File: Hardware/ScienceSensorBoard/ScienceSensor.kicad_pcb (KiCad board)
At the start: 2 copper layers, 2 x 2 mm, 93 parts, among them J1 Conn_02x03_Counter_Clockwise, J2 RJ45_LED_Shielded, Q1 SI4156DY, Q10 BSS138, Q11 SI4156DY, Q2 SI4156DY, Q3 SI4156DY, Q4 BSS138, Q5 BSS138, Q6 BSS138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

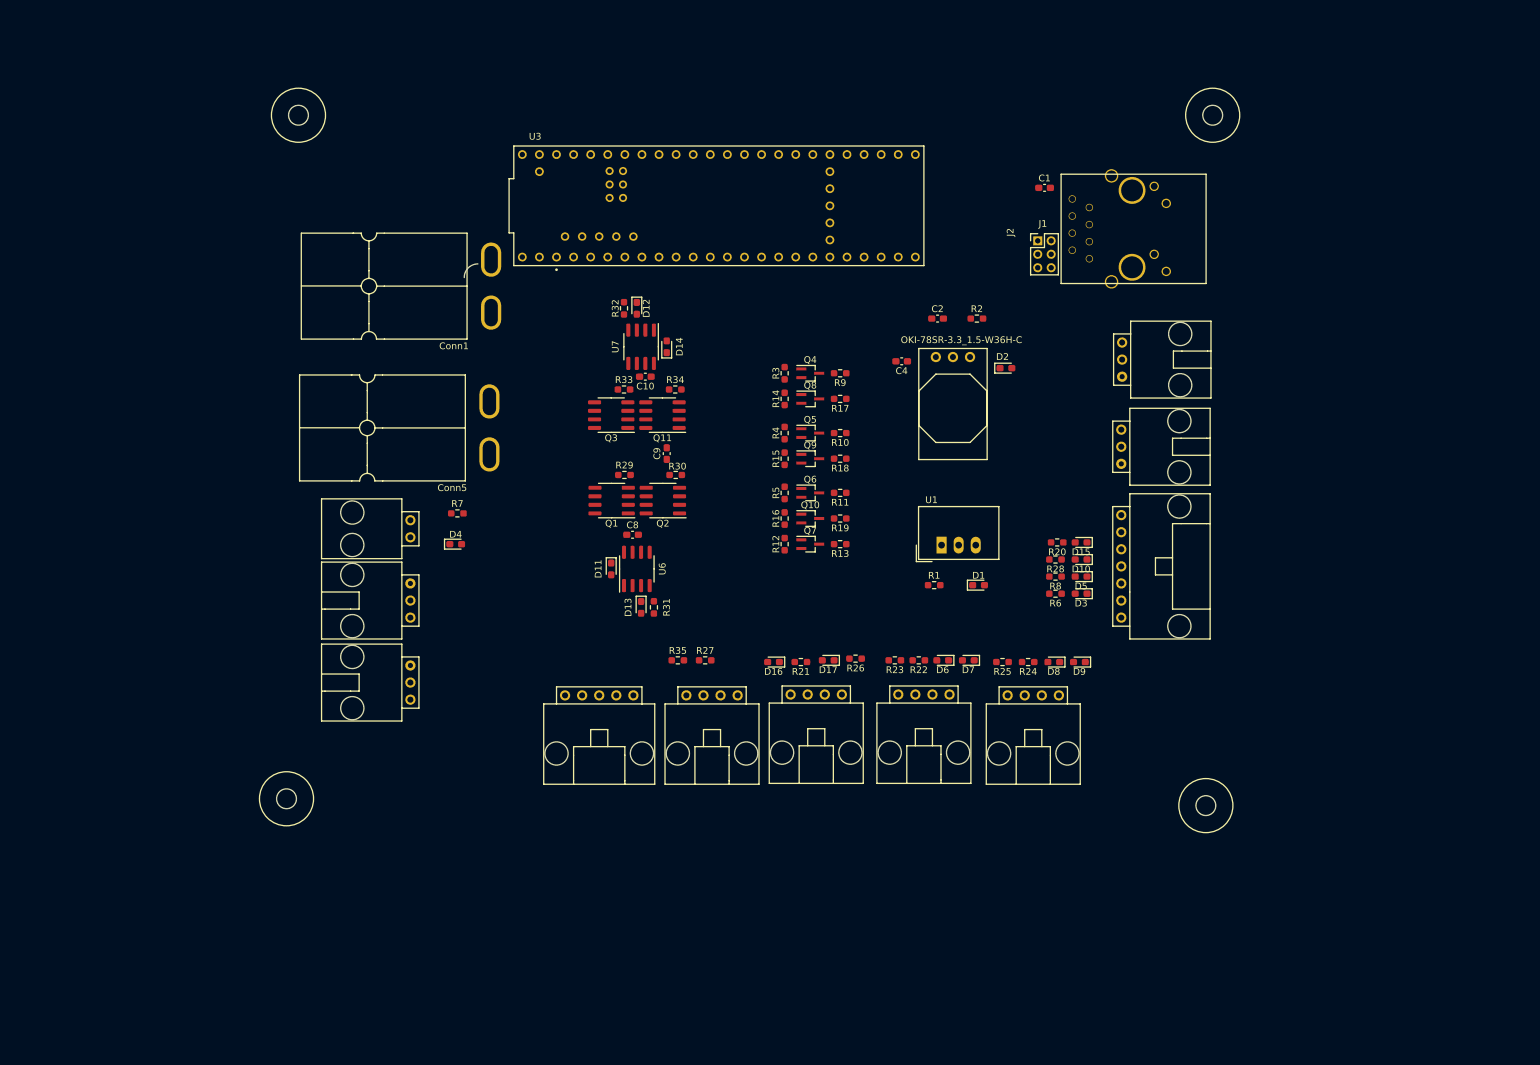
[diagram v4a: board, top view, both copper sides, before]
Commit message: Layout Edge Cuts and Organization
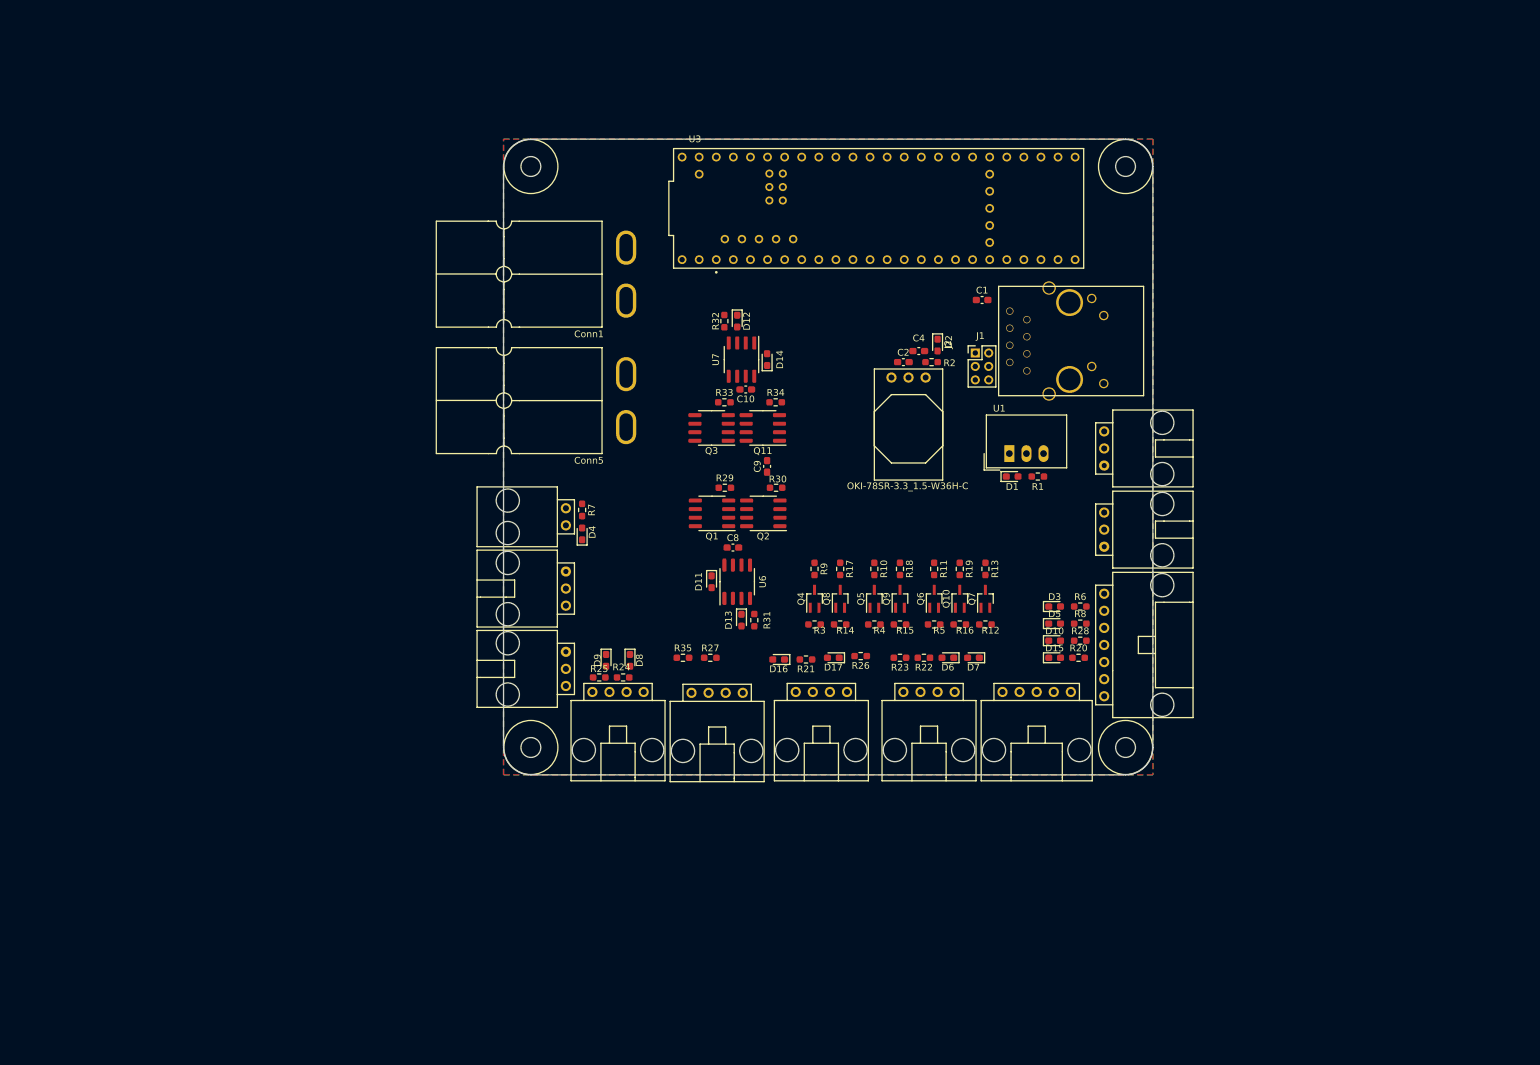
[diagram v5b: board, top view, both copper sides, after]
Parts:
- moved D9 70.4 mm to (111.8, 124.2), turned to -90 degrees
- moved Conn10 65.0 mm to (180.8, 128.9)
- moved D8 63.0 mm to (115.3, 124.2), turned to -90 degrees
- moved Conn9 61.7 mm to (117.3, 128.9)
- moved R24 60.2 mm to (114.3, 126.7)
- moved R25 60.0 mm to (110.7, 126.7)
- moved R3 37.6 mm to (142.7, 118.9), turned to 0 degrees
- moved V4 37.1 mm to (100.6, 137.2)
- moved V1 35.4 mm to (100.6, 50.8)
- moved R14 34.5 mm to (146.6, 118.9), turned to 0 degrees
- moved Q4 33.5 mm to (142.7, 115.1), turned to 90 degrees
- moved R12 32.1 mm to (168.1, 118.9), turned to 0 degrees
- moved R4 31.4 mm to (151.6, 118.9), turned to 0 degrees
- moved R16 30.4 mm to (164.3, 118.9), turned to 0 degrees
- moved Q8 30.0 mm to (146.6, 115.1), turned to 90 degrees
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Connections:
- Conn1 pad 2: (no net) -> +12V
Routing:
- added copper zone on B.Cu, net GND
- added copper zone on F.Cu, net GND
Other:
- board size 2 x 2 mm -> 96.5 x 94.5 mm

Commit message: Layout Wiring
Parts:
- moved Conn2 79.6 mm to (181.0, 101.9), turned to -90 degrees
- moved Conn6 79.5 mm to (108.1, 118.7), turned to 90 degrees
- moved Conn3 78.8 mm to (180.8, 80.0), turned to -90 degrees
- moved Conn4 78.1 mm to (108.1, 106.9), turned to 90 degrees
- moved R20 75.3 mm to (112.5, 94.7), turned to 180 degrees
- moved Conn7 75.2 mm to (181.0, 113.8), turned to -90 degrees
- moved D4 75.1 mm to (178.4, 78.7), turned to -90 degrees
- moved R28 73.8 mm to (112.3, 97.8), turned to 180 degrees
- moved R7 72.9 mm to (178.4, 82.3), turned to 90 degrees
- moved R8 72.3 mm to (112.3, 100.6), turned to 180 degrees
- moved R6 71.1 mm to (112.3, 103.6), turned to 180 degrees
- moved D15 68.8 mm to (116.1, 94.7), turned to 180 degrees
- moved D10 66.6 mm to (116.1, 97.8), turned to 180 degrees
- moved D5 65.2 mm to (115.8, 100.6), turned to 180 degrees
- moved D3 63.9 mm to (115.8, 103.6), turned to 180 degrees
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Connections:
- U3 pad 0: Teensy_O2_RX -> CH4_TX
- U3 pad 1: Teensy_O2_TX -> CH4_RX
- U3 pad 14: LED_260 -> Micro_FWD
- U3 pad 15: LED_275 -> Micro_RVS
- U3 pad 16: LED_280 -> LED_315
- U3 pad 17: LED_315 -> LED_280
- U3 pad 18: unconnected-(U3-Pad18) -> LED_275
- U3 pad 19: unconnected-(U3-Pad19) -> LED_260
- U3 pad 21: unconnected-(U3-Pad21) -> Micro_ENC
- U3 pad 23: Photodiode_1 -> unconnected-(U3-Pad23)
- U3 pad 24: Photodiode_2 -> Photodiode_1
- U3 pad 25: unconnected-(U3-Pad25) -> Photodiode_2
- U3 pad 26: unconnected-(U3-Pad26) -> Micro_Servo
- U3 pad 27: Micro_RVS -> Micro_LIM
- U3 pad 28: CH4_TX -> Teensy_CO2_RX
- U3 pad 29: CH4_RX -> Teensy_CO2_TX
- U3 pad 38: Micro_FWD -> unconnected-(U3-Pad38)
- U3 pad 39: Micro_Servo -> unconnected-(U3-Pad39)
- U3 pad 40: Micro_ENC -> unconnected-(U3-Pad40)
- U3 pad 41: Micro_LIM -> unconnected-(U3-Pad41)
- U3 pad 7: Teensy_CO2_RX -> Teensy_O2_RX
- U3 pad 8: Teensy_CO2_TX -> Teensy_O2_TX
- U3 pad USB_GND1: unconnected-(U3-PadUSB_GND1) -> GND
- U3 pad USB_GND2: unconnected-(U3-PadUSB_GND1) -> GND
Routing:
- net +5V: track 0.00 -> 197.9 mm, vias 0 -> 2
- net +3V3: track 0.00 -> 190.7 mm, vias 0 -> 1
- net +12V: track 0.00 -> 116.5 mm
- net Teensy_CO2_TX: track 0.00 -> 64.4 mm
- net Micro_FWD: track 0.00 -> 63.6 mm, vias 0 -> 4
- net Teensy_CO2_RX: track 0.00 -> 62.5 mm, vias 0 -> 1
- net Micro_RVS: track 0.00 -> 60.5 mm, vias 0 -> 2
- net Photodiode_1: track 0.00 -> 59.6 mm, vias 0 -> 1
- net Teensy_NO2_SCK: track 0.00 -> 57.0 mm, vias 0 -> 1
- net Teensy_NO2_MISO: track 0.00 -> 56.6 mm, vias 0 -> 1
- net Micro_ENC: track 0.00 -> 53.4 mm
- net NH3: track 0.00 -> 53.3 mm
- net Photodiode_2: track 0.00 -> 50.2 mm, vias 0 -> 1
- net LED_315: track 0.00 -> 50.1 mm, vias 0 -> 2
- net Teensy_O2_TX: track 0.00 -> 48.8 mm
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- added copper zone on F.Cu, net /M+
- added copper zone on F.Cu, net /M-

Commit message: Labels
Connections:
- Conn6 pad 1: Micro_ENC -> +12V
- Conn6 pad 2: +12V -> GND
- Conn6 pad 3: GND -> Micro_ENC
- U3 pad USB_GND1: GND -> unconnected-(U3-PadUSB_GND1)
- U3 pad USB_GND2: GND -> unconnected-(U3-PadUSB_GND1)
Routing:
- net +12V: track 116.5 -> 119.6 mm
- net Micro_ENC: track 53.4 -> 55.5 mm
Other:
- board text added: "+ \ + \Heat\Signal"
- board text added: "+ \ -"
- board text added: "+ \ - \ Signal"
- board text added: "+ \ - \ Tx \ Rx"
- board text added: "+ \ - \ x \260\275\280\315"
- board text added: "+ \ - \MISO\CS\SCK"
- board text added: "12V"
- board text added: "CH4"
- board text added: "CO2"
- board text added: "Encoder"
- board text added: "GND"
- board text added: "LEDs"
- board text added: "Limit Switch"
- board text added: "M+"
- board text added: "M-"
- board text added: "NH3"
- board text added: "NO2"
- board text added: "O2"
- board text added: "Photodiode 1"
- board text added: "Photodiode 2"
- board text added: "Servo"
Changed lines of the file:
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@@
   (net 101 "unconnected-(U3-PadVUSB)")
   (net 102 "unconnected-(U3-Pad41)")
+  (net 103 "unconnected-(U3-PadUSB_GND1)")
   (footprint "MRDT_Shields:Teensy_4_1" (layer "F.Cu")
     (at 151.13 79.248 90)
@@
     (pad "T-" thru_hole circle (at -16.24 -1.17 90) (size 1.208 1.208) (drill 0.7) (layers *.Cu *.Mask))
     (pad "USB_GND1" thru_hole circle (at -15.24 4.57 90) (size 1.258 1.258) (drill 0.75) (layers *.Cu *.Mask)
-      (net 4 "GND") (pinfunction "USB_GND") (pintype "power_in+no_connect"))
+      (net 103 "unconnected-(U3-PadUSB_GND1)") (pinfunction "USB_GND") (pintype "power_in+no_connect"))
     (pad "USB_GND2" thru_hole circle (at -12.7 4.57 90) (size 1.258 1.258) (drill 0.75) (layers *.Cu *.Mask)
-      (net 4 "GND") (pinfunction "USB_GND") (pintype "power_in+no_connect"))
+      (net 103 "unconnected-(U3-PadUSB_GND1)") (pinfunction "USB_GND") (pintype "power_in+no_connect"))
     (pad "VBAT" thru_hole circle (at 16.51 5.08 90) (size 1.308 1.308) (drill 0.8) (layers *.Cu *.Mask)
       (net 99 "unconnected-(U3-PadVBAT)") (pinfunction "VBAT") (pintype "passive+no_connect"))
@@
     (pad "" np_thru_hole circle locked (at -1.27 -8.636 90) (size 3.45 3.45) (drill 3.45) (layers *.Cu *.Mask))
     (pad "1" thru_hole circle locked (at 0 0 90) (size 1.524 1.524) (drill 0.9) (layers *.Cu *.Mask)
-      (net 16 "Micro_ENC") (pintype "input"))
-    (pad "2" thru_hole circle locked (at 2.54 0 90) (size 1.524 1.524) (drill 0.9) (layers *.Cu *.Mask)
       (net 3 "+12V") (pintype "input"))
-    (pad "3" thru_hole circle locked (at 5.08 0 90) (size 1.524 1.524) (drill 0.762) (layers *.Cu *.Mask)
+    (pad "2" thru_hole circle locked (at 2.54 0 90) (size 1.524 1.524) (drill 0.9) (layers *.Cu *.Mask)
       (net 4 "GND") (pintype "input"))
+    (pad "3" thru_hole circle locked (at 5.08 0 90) (size 1.524 1.524) (drill 0.762) (layers *.Cu *.Mask)
+      (net 16 "Micro_ENC") (pintype "input"))
     (model "${MRDT_KICAD_LIBRARIES}/3D Files/MRDT_Connctors/Molex_SL_03_Horizontal.stp"
       (offset (xyz 7.619999886 12.95399981 0))
@@
   (gr_arc (start 193.04 137.16) (mid 191.849682 140.033682) (end 188.976 141.224) (layer "Edge.Cuts") (width 0.1))
   (gr_line (start 188.976 141.224) (end 100.584 141.224) (layer "Edge.Cuts") (width 0.1))
+  (gr_text "LEDs" (at 102.616 99.314 270) (layer "B.SilkS")
+    (effects (font (size 1 1) (thickness 0.15)) (justify mirror))
+  )
+  (gr_text "+ \\ - \\ Signal" (at 191.516 116.586 90) (layer "B.SilkS")
+    (effects (font (size 1 1) (thickness 0.15)) (justify mirror))
+  )
+  (gr_text "NO2" (at 175.768 135.382) (layer "B.SilkS")
+    (effects (font (size 1 1) (thickness 0.15)) (justify mirror))
+  )
+  (gr_text "+ \\ - \\ Tx \\ Rx" (at 144.78 139.954) (layer "B.SilkS")
+    (effects (font (size 1 1) (thickness 0.15)) (justify mirror))
+  )
+  (gr_text "+ \\ - \\ Tx \\ Rx" (at 159.766 139.954) (layer "B.SilkS")
+    (effects (font (size 1 1) (thickness 0.15)) (justify mirror))
+  )
+  (gr_text "Limit Switch" (at 187.198 81.28 90) (layer "B.SilkS")
+    (effects (font (size 1 1) (thickness 0.15)) (justify mirror))
+  )
+  (gr_text "+ \\ - \\ Signal" (at 191.516 91.948 90) (layer "B.SilkS")
+    (effects (font (size 1 1) (thickness 0.15)) (justify mirror))
+  )
+  (gr_text "+ \\ -" (at 191.516 81.026 90) (layer "B.SilkS")
+    (effects (font (size 1 1) (thickness 0.15)) (justify mirror))
+  )
+  (gr_text "CO2" (at 159.766 135.382) (layer "B.SilkS")
+    (effects (font (size 1 1) (thickness 0.15)) (justify mirror))
+  )
+  (gr_text "CH4" (at 128.524 135.636) (layer "B.SilkS")
+    (effects (font (size 1 1) (thickness 0.15)) (justify mirror))
+  )
+  (gr_text "+ \\ - \\ Signal" (at 191.516 104.394 90) (layer "B.SilkS")
+    (effects (font (size 1 1) (thickness 0.15)) (justify mirror))
+  )
+  (gr_text "NH3" (at 112.268 135.636) (layer "B.SilkS")
+    (effects (font (size 1 1) (thickness 0.15)) (justify mirror))
+  )
+  (gr_text "Servo" (at 187.198 91.948 90) (layer "B.SilkS")
+    (effects (font (size 1 1) (thickness 0.15)) (justify mirror))
+  )
+  (gr_text "GND" (at 103.632 67.564 270) (layer "B.SilkS")
+    (effects (font (size 1 1) (thickness 0.15)) (justify mirror))
+  )
+  (gr_text "Encoder" (at 102.87 115.824 270) (layer "B.SilkS")
+    (effects (font (size 1 1) (thickness 0.15)) (justify mirror))
+  )
+  (gr_text "+ \\ - \\ Tx \\ Rx" (at 128.524 139.954) (layer "B.SilkS")
+    (effects (font (size 1 1) (thickness 0.15)) (justify mirror))
+  )
+  (gr_text "M-" (at 104.14 83.566 270) (layer "B.SilkS")
+    (effects (font (size 1 1) (thickness 0.15)) (justify mirror))
+  )
+  (gr_text "+ \\ - \\MISO\\CS\\SCK" (at 175.768 139.954) (layer "B.SilkS")
+    (effects (font (size 1 1) (thickness 0.15)) (justify mirror))
+  )
+  (gr_text "O2" (at 144.526 135.382) (layer "B.SilkS")
+    (effects (font (size 1 1) (thickness 0.15)) (justify mirror))
+  )
+  (gr_text "M+" (at 104.14 76.2 270) (layer "B.SilkS")
+    (effects (font (size 1 1) (thickness 0.15)) (justify mirror))
+  )
+  (gr_text "+ \\ + \\Heat\\Signal" (at 112.522 139.954) (layer "B.SilkS")
+    (effects (font (size 1 1) (thickness 0.15)) (justify mirror))
+  )
+  (gr_text "Photodiode 2" (at 186.944 104.14 90) (layer "B.SilkS")
+    (effects (font (size 1 1) (thickness 0.15)) (justify mirror))
+  )
+  (gr_text "12V" (at 103.886 59.182 270) (layer "B.SilkS")
+    (effects (font (size 1 1) (thickness 0.15)) (justify mirror))
+  )
+  (gr_text "+ \\ - \\ x \\260\\275\\280\\315" (at 98.298 99.06 270) (layer "B.SilkS")
+    (effects (font (size 1 1) (thickness 0.15)) (justify mirror))
+  )
+  (gr_text "+ \\ - \\ Signal" (at 98.298 116.332 270) (layer "B.SilkS")
+    (effects (font (size 1 1) (thickness 0.15)) (justify mirror))
+  )
+  (gr_text "Photodiode 1" (at 186.944 116.332 90) (layer "B.SilkS")
+    (effects (font (size 1 1) (thickness 0.15)) (justify mirror))
+  )
   (segment (start 170.0915 61.226) (end 172.1485 61.226) (width 0.254) (layer "F.Cu") (net 1))
   (segment (start 166.7775 57.912) (end 170.0915 61.226) (width 0.254) (layer "F.Cu") (net 1))
@@
   (segment (start 118.429 106.934) (end 115.062 106.934) (width 0.762) (layer "F.Cu") (net 3))
   (segment (start 124.065 79.135) (end 120.523 82.677) (width 0.762) (layer "F.Cu") (net 3))
-  (segment (start 108.077 106.934) (end 106.734 108.277) (width 0.762) (layer "F.Cu") (net 3))
   (segment (start 129.348 77.535) (end 129.348 74.277466) (width 0.762) (layer "F.Cu") (net 3))
-  (segment (start 106.734 108.277) (end 106.734 114.862) (width 0.762) (layer "F.Cu") (net 3))
+  (segment (start 106.063901 108.947099) (end 106.063901 116.731901) (width 0.762) (layer "F.Cu") (net 3))
   (segment (start 114.6874 67.352) (end 125.713 67.352) (width 0.762) (layer "F.Cu") (net 3))
   (segment (start 128.48679 79.135) (end 126.87921 79.135) (width 0.762) (layer "F.Cu") (net 3))
+  (segment (start 106.063901 116.731901) (end 108.077 118.745) (width 0.762) (layer "F.Cu") (net 3))
   (segment (start 125.815 70.744466) (end 129.348 74.277466) (width 0.762) (layer "F.Cu") (net 3))
   (segment (start 125.815 58.886) (end 124.079 57.15) (width 0.762) (layer "F.Cu") (net 3))
@@
   (segment (start 120.523 82.677) (end 120.523 92.075) (width 0.762) (layer "F.Cu") (net 3))
   (segment (start 124.598 115.505) (end 122.998 113.905) (width 0.762) (layer "F.Cu") (net 3))
+  (segment (start 108.077 106.934) (end 106.063901 108.947099) (width 0.762) (layer "F.Cu") (net 3))
   (segment (start 124.903 115.505) (end 124.598 115.505) (width 0.762) (layer "F.Cu") (net 3))
   (segment (start 126.87921 79.135) (end 124.065 79.135) (width 0.762) (layer "F.Cu") (net 3))
@@
   (segment (start 120.588 104.775) (end 118.429 106.934) (width 0.762) (layer "F.Cu") (net 3))
   (segment (start 126.87921 79.135) (end 131.253 79.135) (width 0.762) (layer "F.Cu") (net 3))
-  (segment (start 106.734 114.862) (end 108.077 116.205) (width 0.762) (layer "F.Cu") (net 3))
   (segment (start 129.348 74.277466) (end 125.809534 70.739) (width 0.762) (layer "F.Cu") (net 3))
   (segment (start 129.348 78.27379) (end 128.48679 79.135) (width 0.762) (layer "F.Cu") (net 3))
@@
   (segment (start 131.918 99.984) (end 120.05 99.984) (width 0.254) (layer "B.Cu") (net 15))
   (segment (start 120.05 99.984) (end 113.538 93.472) (width 0.254) (layer "B.Cu") (net 15))
-  (segment (start 137.16 111.277324) (end 137.16 99.568) (width 0.254) (layer "F.Cu") (net 16))
+  (segment (start 137.16 99.568) (end 140.97 95.758) (width 0.254) (layer "F.Cu") (net 16))
   (segment (start 127.787324 120.65) (end 137.16 111.277324) (width 0.254) (layer "F.Cu") (net 16))
+  (segment (start 108.077 113.665) (end 115.062 120.65) (width 0.254) (layer "F.Cu") (net 16))
   (segment (start 140.97 95.758) (end 143.51 95.758) (width 0.254) (layer "F.Cu") (net 16))
-  (segment (start 137.16 99.568) (end 140.97 95.758) (width 0.254) (layer "F.Cu") (net 16))
-  (segment (start 108.077 118.745) (end 109.982 120.65) (width 0.254) (layer "F.Cu") (net 16))
-  (segment (start 109.982 120.65) (end 127.787324 120.65) (width 0.254) (layer "F.Cu") (net 16))
+  (segment (start 137.16 111.277324) (end 137.16 99.568) (width 0.254) (layer "F.Cu") (net 16))
+  (segment (start 115.062 120.65) (end 127.787324 120.65) (width 0.254) (layer "F.Cu") (net 16))
   (segment (start 156.21 122.9595) (end 160.147 122.9595) (width 0.381) (layer "F.Cu") (net 17))
   (segment (start 148.336 128.905) (end 149.097999 128.143001) (width 0.381) (layer "F.Cu") (net 17))

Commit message: Logo and Names, rearranging for better ground
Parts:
- added G***: LOGO, MRDT_Silkscreens:0_MRDT_Logo_7.5mm, F.Cu at (169.9, 80.0)
- moved Conn6 2.16 mm to (108.1, 120.9)
- moved Conn4 1.53 mm to (108.0, 108.5)
- moved D16 1.40 mm to (130.8, 124.5)
- moved C1 1.37 mm to (168.9, 58.5)
- moved J2 1.37 mm to (194.9, 64.5)
- moved J1 1.37 mm to (167.8, 66.4)
- moved Conn5 1.27 mm to (115.1, 76.7)
- moved R25 1.27 mm to (140.5, 126.7)
- moved Conn1 1.10 mm to (115.1, 60.0)
- moved R24 0.76 mm to (144.5, 126.7)
- moved V1 0.51 mm to (100.6, 51.3)
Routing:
- net O2_RX: track 15.0 -> 16.5 mm
- net +12V: track 119.6 -> 120.9 mm
- net +5V: track 197.9 -> 196.6 mm
- net Micro_ENC: track 55.5 -> 54.6 mm
- net LED_275: track 44.6 -> 43.7 mm
- net Net-(D9-Pad2): track 1.71 -> 2.23 mm
- net LED_315: track 50.1 -> 49.6 mm
- net LED_280: track 47.6 -> 47.1 mm
- net LED_260: track 43.2 -> 42.7 mm
- net GND: vias 21 -> 24
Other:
- board text added: "Science Sensor Board, 2023 Rev 1 Mars Rover Design Team A.J Lee, Sean Tillmon"
